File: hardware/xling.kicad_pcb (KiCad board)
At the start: 2 copper layers, 45 x 60 mm, 54 parts, among them J3 MCP73831, J4 USB_OTG, J5 AVR ISP, J6 Battery, Q1 TP0610T, SW2 Up, SW3 Select, SW4 Down, U1 LT1109CZ-12, U2 ATMEGA328P-AU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

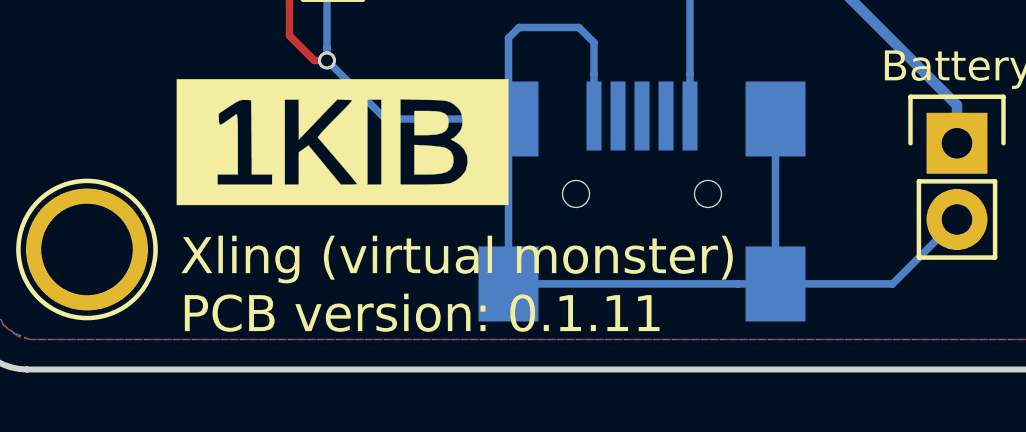
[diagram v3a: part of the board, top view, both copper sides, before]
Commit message: patch 0.1.12: Remove all dummy elements from PCB design.
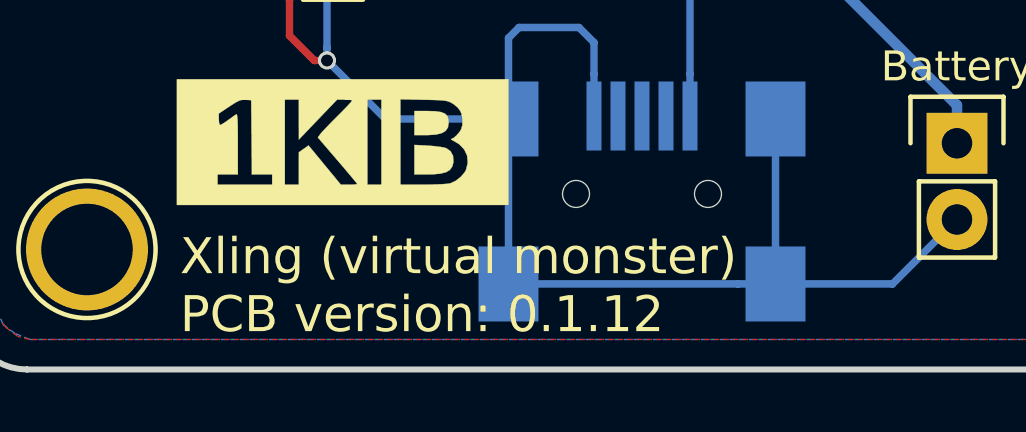
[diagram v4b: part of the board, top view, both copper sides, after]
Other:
- board text added: "Xling (virtual monster) PCB version: 0.1.12"
- board text removed: "Xling (virtual monster) PCB version: 0.1.11"
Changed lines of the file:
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@@
 (kicad_pcb (version 4) (host pcbnew 4.0.7)
   (general
-    (links 0)
+    (links 127)
     (no_connects 0)
-    (area 118.899999 77.899999 164.100001 138.100001)
+    (area 118.651905 76.125 172.20762 138.100001)
     (thickness 1.6)
-    (drawings 22)
+    (drawings 12)
     (tracks 704)
     (zones 0)
@@
       (effects (font (size 1 1) (thickness 0.15)))
     )
-    (fp_text value DEP_128064I (at 0 4.09 180) (layer F.Fab)
+    (fp_text value DEP_128064I (at 0 4.09 180) (layer F.Fab) hide
       (effects (font (size 1 1) (thickness 0.15)))
     )
@@
       (xy 2.413 -0.211667) (xy 2.413 -1.016) (xy 2.838435 -1.016) (xy 3.106894 -1.008133)) (layer F.SilkS) (width 0.01))
   )
-  (gr_text "Xling (virtual monster)\nPCB version: 0.1.11" (at 126.1 135.2) (layer F.SilkS)
+  (gr_text "Xling (virtual monster)\nPCB version: 0.1.12" (at 126.1 135.2) (layer F.SilkS)
     (effects (font (size 1.2 1.2) (thickness 0.25)) (justify left))
-  )
-  (gr_line (start 116 117) (end 167 117) (layer B.Fab) (width 0.1))
-  (gr_line (start 116 119) (end 167 119) (layer B.Fab) (width 0.1))
-  (dimension 27 (width 0.3) (layer F.SilkS)
-    (gr_text "27.000 mm" (at 141.5 145.65) (layer F.SilkS)
-      (effects (font (size 1.5 1.5) (thickness 0.3)))
-    )
-    (feature1 (pts (xy 155 117) (xy 155 147)))
-    (feature2 (pts (xy 128 117) (xy 128 147)))
-    (crossbar (pts (xy 128 144.3) (xy 155 144.3)))
-    (arrow1a (pts (xy 155 144.3) (xy 153.873496 144.886421)))
-    (arrow1b (pts (xy 155 144.3) (xy 153.873496 143.713579)))
-    (arrow2a (pts (xy 128 144.3) (xy 129.126504 144.886421)))
-    (arrow2b (pts (xy 128 144.3) (xy 129.126504 143.713579)))
-  )
-  (dimension 21 (width 0.3) (layer F.SilkS)
-    (gr_text "21.000 mm" (at 174.55 127.5 90) (layer F.SilkS)
-      (effects (font (size 1.5 1.5) (thickness 0.3)))
-    )
-    (feature1 (pts (xy 141.5 117) (xy 175.9 117)))
-    (feature2 (pts (xy 141.5 138) (xy 175.9 138)))
-    (crossbar (pts (xy 173.2 138) (xy 173.2 117)))
-    (arrow1a (pts (xy 173.2 117) (xy 173.786421 118.126504)))
-    (arrow1b (pts (xy 173.2 117) (xy 172.613579 118.126504)))
-    (arrow2a (pts (xy 173.2 138) (xy 173.786421 136.873496)))
-    (arrow2b (pts (xy 173.2 138) (xy 172.613579 136.873496)))
-  )
-  (dimension 19 (width 0.3) (layer F.SilkS)
-    (gr_text "19.000 mm" (at 170.05 128.5 90) (layer F.SilkS)
-      (effects (font (size 1.5 1.5) (thickness 0.3)))
-    )
-    (feature1 (pts (xy 141.5 119) (xy 171.4 119)))
-    (feature2 (pts (xy 141.5 138) (xy 171.4 138)))
-    (crossbar (pts (xy 168.7 138) (xy 168.7 119)))
-    (arrow1a (pts (xy 168.7 119) (xy 169.286421 120.126504)))
-    (arrow1b (pts (xy 168.7 119) (xy 168.113579 120.126504)))
-    (arrow2a (pts (xy 168.7 138) (xy 169.286421 136.873496)))
-    (arrow2b (pts (xy 168.7 138) (xy 168.113579 136.873496)))
-  )
-  (dimension 52 (width 0.3) (layer F.SilkS)
-    (gr_text "52.000 mm" (at 114.65 108 90) (layer F.SilkS)
-      (effects (font (size 1.5 1.5) (thickness 0.3)))
-    )
-    (feature1 (pts (xy 123 82) (xy 113.3 82)))
-    (feature2 (pts (xy 123 134) (xy 113.3 134)))
-    (crossbar (pts (xy 116 134) (xy 116 82)))
-    (arrow1a (pts (xy 116 82) (xy 116.586421 83.126504)))
-    (arrow1b (pts (xy 116 82) (xy 115.413579 83.126504)))
-    (arrow2a (pts (xy 116 134) (xy 116.586421 132.873496)))
-    (arrow2b (pts (xy 116 134) (xy 115.413579 132.873496)))
-  )
-  (dimension 37.000135 (width 0.3) (layer F.SilkS)
-    (gr_text "37.000 mm" (at 141.452834 151.501227 359.8451469) (layer F.SilkS)
-      (effects (font (size 1.5 1.5) (thickness 0.3)))
-    )
-    (feature1 (pts (xy 160 134.1) (xy 159.949186 152.901222)))
-    (feature2 (pts (xy 123 134) (xy 122.949186 152.801222)))
-    (crossbar (pts (xy 122.956483 150.101232) (xy 159.956483 150.201232)))
-    (arrow1a (pts (xy 159.956483 150.201232) (xy 158.828398 150.784606)))
-    (arrow1b (pts (xy 159.956483 150.201232) (xy 158.831568 149.611769)))
-    (arrow2a (pts (xy 122.956483 150.101232) (xy 124.081398 150.690695)))
-    (arrow2b (pts (xy 122.956483 150.101232) (xy 124.084568 149.517858)))
-  )
-  (dimension 60 (width 0.3) (layer F.SilkS)
-    (gr_text "60.000 mm" (at 108.45 108 90) (layer F.SilkS)
-      (effects (font (size 1.5 1.5) (thickness 0.3)))
-    )
-    (feature1 (pts (xy 119 78) (xy 107.1 78)))
-    (feature2 (pts (xy 119 138) (xy 107.1 138)))
-    (crossbar (pts (xy 109.8 138) (xy 109.8 78)))
-    (arrow1a (pts (xy 109.8 78) (xy 110.386421 79.126504)))
-    (arrow1b (pts (xy 109.8 78) (xy 109.213579 79.126504)))
-    (arrow2a (pts (xy 109.8 138) (xy 110.386421 136.873496)))
-    (arrow2b (pts (xy 109.8 138) (xy 109.213579 136.873496)))
-  )
-  (dimension 45 (width 0.3) (layer F.SilkS)
-    (gr_text "45.000 mm" (at 141.5 156.75) (layer F.SilkS)
-      (effects (font (size 1.5 1.5) (thickness 0.3)))
-    )
-    (feature1 (pts (xy 164 138) (xy 164 158.1)))
-    (feature2 (pts (xy 119 138) (xy 119 158.1)))
-    (crossbar (pts (xy 119 155.4) (xy 164 155.4)))
-    (arrow1a (pts (xy 164 155.4) (xy 162.873496 155.986421)))
-    (arrow1b (pts (xy 164 155.4) (xy 162.873496 154.813579)))
-    (arrow2a (pts (xy 119 155.4) (xy 120.126504 155.986421)))
-    (arrow2b (pts (xy 119 155.4) (xy 120.126504 154.813579)))
   )
   (target plus (at 160 134) (size 5) (width 0.2) (layer Edge.Cuts))
   (target plus (at 160 82) (size 5) (width 0.2) (layer Edge.Cuts))
   (target plus (at 123 134) (size 5) (width 0.2) (layer Edge.Cuts))
-  (gr_line (start 141.5 75) (end 141.5 141) (layer B.Fab) (width 0.1))
   (gr_arc (start 121 80) (end 119 80) (angle 90) (layer Edge.Cuts) (width 0.2))
   (gr_arc (start 162 80) (end 162 78) (angle 90) (layer Edge.Cuts) (width 0.2))

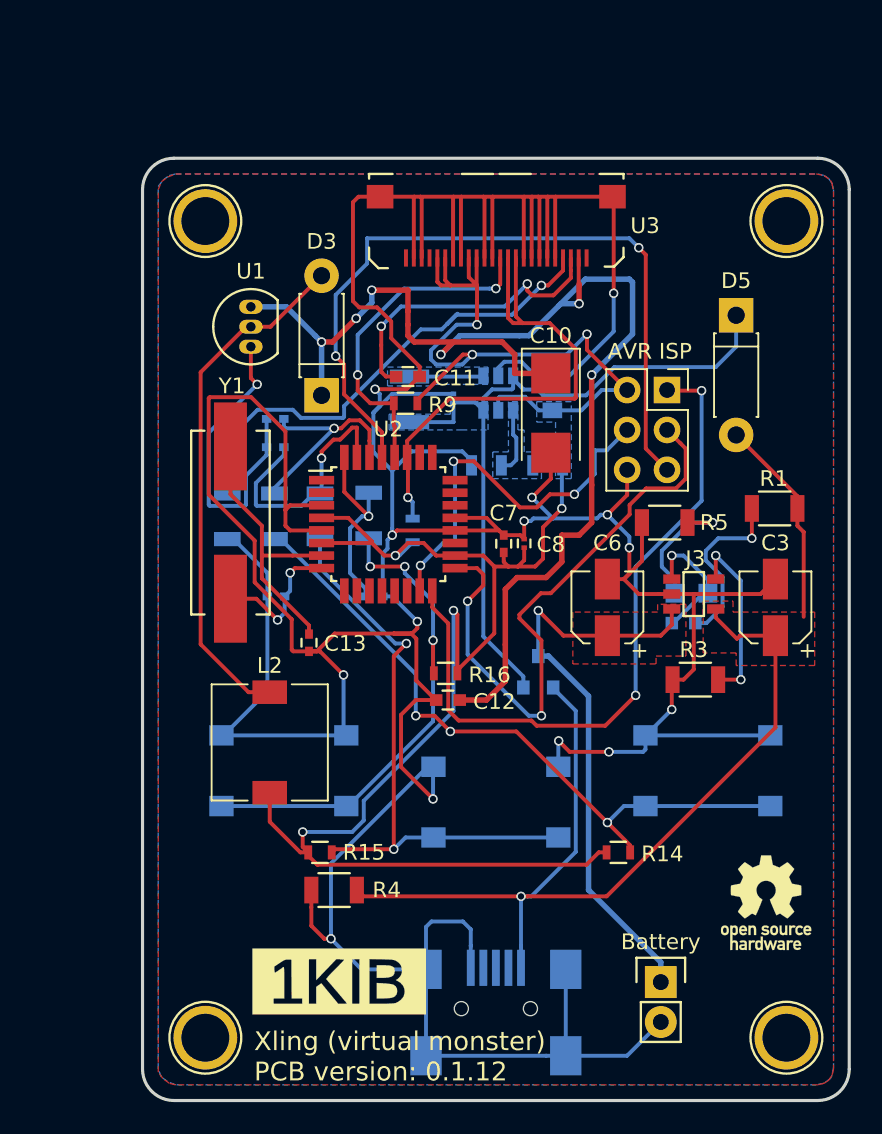
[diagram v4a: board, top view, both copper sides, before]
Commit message: patch 0.1.13: Adjust silk screen text to include into Gerber files.
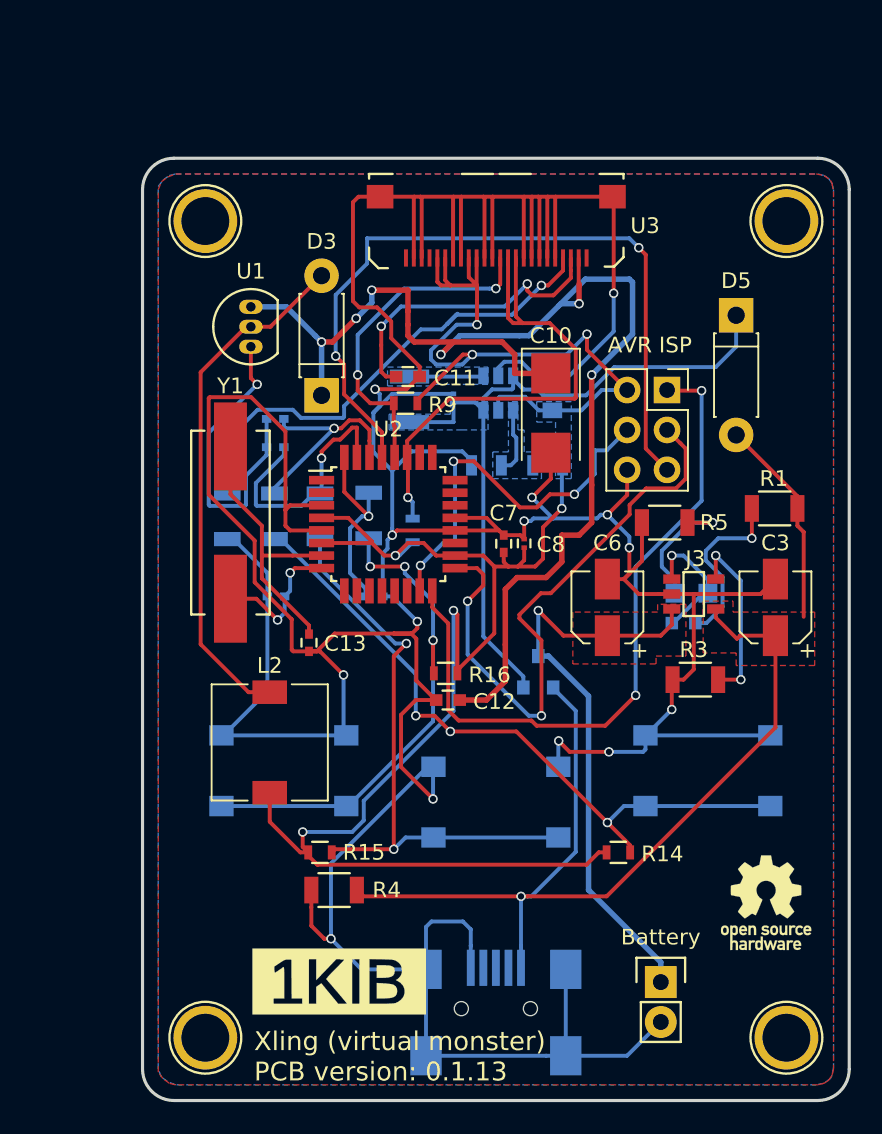
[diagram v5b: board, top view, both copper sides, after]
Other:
- board text added: "AVR ISP"
- board text added: "Battery"
- board text added: "Down"
- board text added: "Select"
- board text added: "Up"
- board text added: "Xling (virtual monster) PCB version: 0.1.13"
- board text added: "charged"
- board text added: "charging"
- board text removed: "Xling (virtual monster) PCB version: 0.1.12"
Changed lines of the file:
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@@
     (links 127)
     (no_connects 0)
-    (area 118.651905 76.125 172.20762 138.100001)
+    (area 99.150001 72.5 186.25 157.600001)
     (thickness 1.6)
-    (drawings 12)
+    (drawings 26)
     (tracks 704)
     (zones 0)
@@
     (pad_drill 0.762)
     (pad_to_mask_clearance 0.2)
-    (aux_axis_origin 123 134)
-    (grid_origin 123 134)
+    (solder_mask_min_width 0.1)
+    (pad_to_paste_clearance_ratio -0.05)
+    (aux_axis_origin 114 141)
+    (grid_origin 114 141)
     (visible_elements FFFFFF7F)
     (pcbplotparams
-      (layerselection 0x00030_80000001)
-      (usegerberextensions false)
+      (layerselection 0x010fc_80000001)
+      (usegerberextensions true)
       (excludeedgelayer true)
       (linewidth 0.100000)
@@
       (psa4output false)
       (plotreference true)
-      (plotvalue true)
+      (plotvalue false)
       (plotinvisibletext false)
       (padsonsilk false)
@@
       (outputformat 1)
       (mirror false)
-      (drillshape 1)
+      (drillshape 0)
       (scaleselection 1)
-      (outputdirectory ""))
+      (outputdirectory gerber/))
   )
   (net 0 "")
@@
       (effects (font (size 1 1) (thickness 0.15)) (justify mirror))
     )
-    (fp_text value charging (at 5.7507 0.2) (layer B.SilkS)
+    (fp_text value charging (at 5.7507 0.2) (layer B.SilkS) hide
       (effects (font (size 1 1) (thickness 0.15)) (justify mirror))
     )
@@
       (effects (font (size 1 1) (thickness 0.15)) (justify mirror))
     )
-    (fp_text value charged (at 5.00098 0) (layer B.SilkS)
+    (fp_text value charged (at 5.00098 0) (layer B.SilkS) hide
       (effects (font (size 1 1) (thickness 0.15)) (justify mirror))
     )
@@
       (effects (font (size 1 1) (thickness 0.15)))
     )
-    (fp_text value Battery (at 0 -2.56 180) (layer F.SilkS)
+    (fp_text value Battery (at 0 -2.56) (layer F.SilkS) hide
       (effects (font (size 1 1) (thickness 0.15)))
     )
@@
     (tags "Crystal Quarz HC49-SD SMD")
     (attr smd)
-    (fp_text reference Y1 (at 8.7 0.1 180) (layer F.SilkS)
+    (fp_text reference Y1 (at 8.7 0 180) (layer F.SilkS)
       (effects (font (size 1 1) (thickness 0.15)))
     )
@@
       (effects (font (size 1 1) (thickness 0.15)))
     )
-    (fp_text value "AVR ISP" (at -1.1 -2.46 180) (layer F.SilkS)
+    (fp_text value "AVR ISP" (at -1.1 -2.46) (layer F.SilkS) hide
       (effects (font (size 1 1) (thickness 0.15)))
     )
@@
       (effects (font (size 1 1) (thickness 0.15)) (justify mirror))
     )
-    (fp_text value Up (at 0 -4.15) (layer B.SilkS)
+    (fp_text value Up (at 0 -4.15) (layer B.SilkS) hide
       (effects (font (size 1 1) (thickness 0.15)) (justify mirror))
     )
@@
       (effects (font (size 1 1) (thickness 0.15)) (justify mirror))
     )
-    (fp_text value Select (at 0 -4.15) (layer B.SilkS)
+    (fp_text value Select (at 0 -4.15) (layer B.SilkS) hide
       (effects (font (size 1 1) (thickness 0.15)) (justify mirror))
     )
@@
       (effects (font (size 1 1) (thickness 0.15)) (justify mirror))
     )
-    (fp_text value Down (at 0 -4.15) (layer B.SilkS)
+    (fp_text value Down (at 0 -4.15) (layer B.SilkS) hide
       (effects (font (size 1 1) (thickness 0.15)) (justify mirror))
     )
@@
       (xy 2.413 -0.211667) (xy 2.413 -1.016) (xy 2.838435 -1.016) (xy 3.106894 -1.008133)) (layer F.SilkS) (width 0.01))
   )
-  (gr_text "Xling (virtual monster)\nPCB version: 0.1.12" (at 126.1 135.2) (layer F.SilkS)
+  (gr_text charging (at 159.2 107.8) (layer B.SilkS)
+    (effects (font (size 1 1) (thickness 0.2)) (justify mirror))
+  )
+  (gr_text charged (at 159 105.7) (layer B.SilkS)
+    (effects (font (size 1 1) (thickness 0.2)) (justify mirror))
+  )
+  (gr_text Up (at 155 112.8) (layer B.SilkS)
+    (effects (font (size 1 1) (thickness 0.2)) (justify mirror))
+  )
+  (gr_text Select (at 141.5 114.8) (layer B.SilkS)
+    (effects (font (size 1 1) (thickness 0.2)) (justify mirror))
+  )
+  (gr_text Down (at 128 112.8) (layer B.SilkS)
+    (effects (font (size 1 1) (thickness 0.2)) (justify mirror))
+  )
+  (gr_text "AVR ISP" (at 151.3 89.9) (layer F.SilkS)
+    (effects (font (size 1 1) (thickness 0.2)))
+  )
+  (gr_text Battery (at 152 127.6) (layer F.SilkS)
+    (effects (font (size 1 1) (thickness 0.2)))
+  )
+  (dimension 21 (width 0.3) (layer B.Fab)
+    (gr_text "21.000 mm" (at 179.75 127.5 270) (layer B.Fab)
+      (effects (font (size 1.5 1.5) (thickness 0.3)))
+    )
+    (feature1 (pts (xy 128 138) (xy 181.1 138)))
+    (feature2 (pts (xy 128 117) (xy 181.1 117)))
+    (crossbar (pts (xy 178.4 117) (xy 178.4 138)))
+    (arrow1a (pts (xy 178.4 138) (xy 177.813579 136.873496)))
+    (arrow1b (pts (xy 178.4 138) (xy 178.986421 136.873496)))
+    (arrow2a (pts (xy 178.4 117) (xy 177.813579 118.126504)))
+    (arrow2b (pts (xy 178.4 117) (xy 178.986421 118.126504)))
+  )
+  (dimension 19 (width 0.3) (layer B.Fab)
+    (gr_text "19.000 mm" (at 174.15 128.5 270) (layer B.Fab)
+      (effects (font (size 1.5 1.5) (thickness 0.3)))
+    )
+    (feature1 (pts (xy 141.5 138) (xy 175.5 138)))
+    (feature2 (pts (xy 141.5 119) (xy 175.5 119)))
+    (crossbar (pts (xy 172.8 119) (xy 172.8 138)))
+    (arrow1a (pts (xy 172.8 138) (xy 172.213579 136.873496)))
+    (arrow1b (pts (xy 172.8 138) (xy 173.386421 136.873496)))
+    (arrow2a (pts (xy 172.8 119) (xy 172.213579 120.126504)))
+    (arrow2b (pts (xy 172.8 119) (xy 173.386421 120.126504)))
+  )
+  (dimension 27 (width 0.3) (layer B.Fab)
+    (gr_text "27.000 mm" (at 141.5 146.85) (layer B.Fab)
+      (effects (font (size 1.5 1.5) (thickness 0.3)))
+    )
+    (feature1 (pts (xy 155 117) (xy 155 148.2)))
+    (feature2 (pts (xy 128 117) (xy 128 148.2)))
+    (crossbar (pts (xy 128 145.5) (xy 155 145.5)))
+    (arrow1a (pts (xy 155 145.5) (xy 153.873496 146.086421)))
+    (arrow1b (pts (xy 155 145.5) (xy 153.873496 144.913579)))
+    (arrow2a (pts (xy 128 145.5) (xy 129.126504 146.086421)))
+    (arrow2b (pts (xy 128 145.5) (xy 129.126504 144.913579)))
+  )
+  (dimension 52 (width 0.3) (layer B.Fab)
+    (gr_text "52.000 mm" (at 111.75 108 90) (layer B.Fab)
+      (effects (font (size 1.5 1.5) (thickness 0.3)))
+    )
+    (feature1 (pts (xy 123 82) (xy 110.4 82)))
+    (feature2 (pts (xy 123 134) (xy 110.4 134)))
+    (crossbar (pts (xy 113.1 134) (xy 113.1 82)))
+    (arrow1a (pts (xy 113.1 82) (xy 113.686421 83.126504)))
+    (arrow1b (pts (xy 113.1 82) (xy 112.513579 83.126504)))
+    (arrow2a (pts (xy 113.1 134) (xy 113.686421 132.873496)))
+    (arrow2b (pts (xy 113.1 134) (xy 112.513579 132.873496)))
+  )
+  (dimension 37 (width 0.3) (layer B.Fab)
+    (gr_text "37.000 mm" (at 141.5 151.85) (layer B.Fab)
+      (effects (font (size 1.5 1.5) (thickness 0.3)))
+    )
+    (feature1 (pts (xy 160 134) (xy 160 153.2)))
+    (feature2 (pts (xy 123 134) (xy 123 153.2)))
+    (crossbar (pts (xy 123 150.5) (xy 160 150.5)))
+    (arrow1a (pts (xy 160 150.5) (xy 158.873496 151.086421)))
+    (arrow1b (pts (xy 160 150.5) (xy 158.873496 149.913579)))
+    (arrow2a (pts (xy 123 150.5) (xy 124.126504 151.086421)))
+    (arrow2b (pts (xy 123 150.5) (xy 124.126504 149.913579)))
+  )
+  (dimension 60 (width 0.3) (layer B.Fab)
+    (gr_text "60.000 mm" (at 105.65 108 90) (layer B.Fab)
+      (effects (font (size 1.5 1.5) (thickness 0.3)))
+    )
+    (feature1 (pts (xy 121 78) (xy 104.3 78)))
+    (feature2 (pts (xy 121 138) (xy 104.3 138)))
+    (crossbar (pts (xy 107 138) (xy 107 78)))
+    (arrow1a (pts (xy 107 78) (xy 107.586421 79.126504)))
+    (arrow1b (pts (xy 107 78) (xy 106.413579 79.126504)))
+    (arrow2a (pts (xy 107 138) (xy 107.586421 136.873496)))
+    (arrow2b (pts (xy 107 138) (xy 106.413579 136.873496)))
+  )
+  (dimension 45 (width 0.3) (layer B.Fab)
+    (gr_text "45.000 mm" (at 141.5 156.25) (layer B.Fab)
+      (effects (font (size 1.5 1.5) (thickness 0.3)))
+    )
+    (feature1 (pts (xy 164 136) (xy 164 157.6)))
+    (feature2 (pts (xy 119 136) (xy 119 157.6)))
+    (crossbar (pts (xy 119 154.9) (xy 164 154.9)))
+    (arrow1a (pts (xy 164 154.9) (xy 162.873496 155.486421)))
+    (arrow1b (pts (xy 164 154.9) (xy 162.873496 154.313579)))
+    (arrow2a (pts (xy 119 154.9) (xy 120.126504 155.486421)))
+    (arrow2b (pts (xy 119 154.9) (xy 120.126504 154.313579)))
+  )
+  (target plus (at 169 75) (size 5) (width 0.2) (layer Edge.Cuts))
+  (target plus (at 169 141) (size 5) (width 0.2) (layer Edge.Cuts))
+  (target plus (at 114 141) (size 5) (width 0.2) (layer Edge.Cuts))
+  (gr_text "Xling (virtual monster)\nPCB version: 0.1.13" (at 126.1 135.2) (layer F.SilkS)
     (effects (font (size 1.2 1.2) (thickness 0.25)) (justify left))
   )
-  (target plus (at 160 134) (size 5) (width 0.2) (layer Edge.Cuts))
-  (target plus (at 160 82) (size 5) (width 0.2) (layer Edge.Cuts))
-  (target plus (at 123 134) (size 5) (width 0.2) (layer Edge.Cuts))
   (gr_arc (start 121 80) (end 119 80) (angle 90) (layer Edge.Cuts) (width 0.2))
   (gr_arc (start 162 80) (end 162 78) (angle 90) (layer Edge.Cuts) (width 0.2))
